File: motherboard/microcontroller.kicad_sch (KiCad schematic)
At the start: 5 parts, among them SW1 SW_Push, SW2 SW_Push, U3 ESP32-S3-WROOM-1

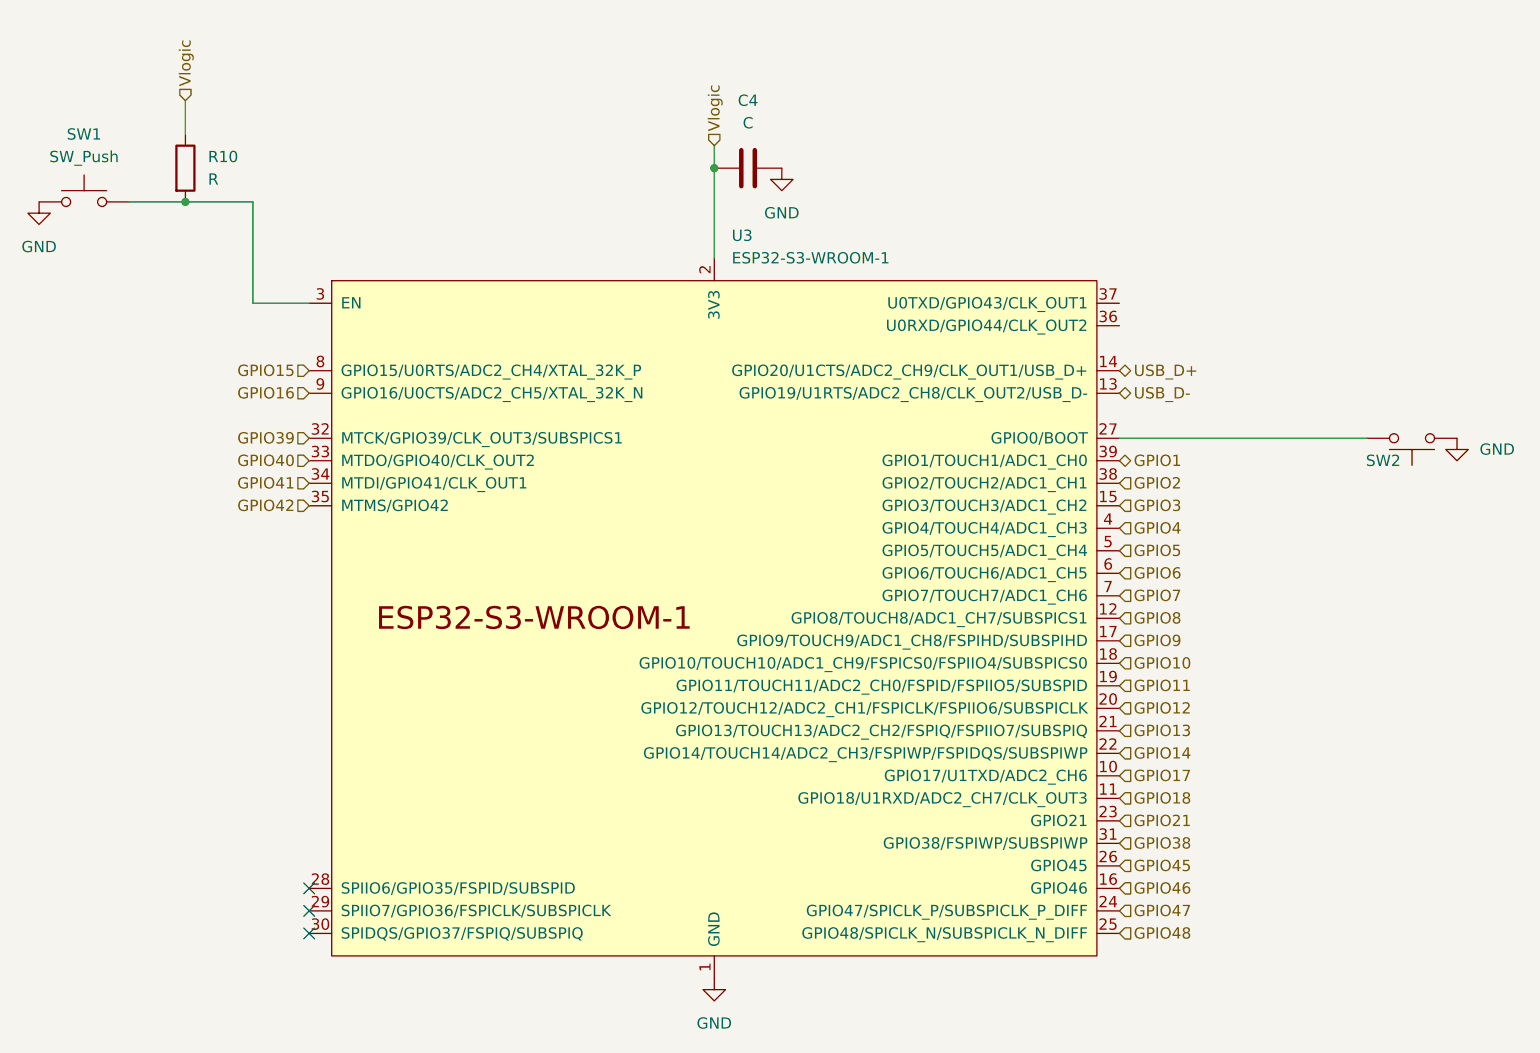
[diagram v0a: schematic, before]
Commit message: motherboard basics routed
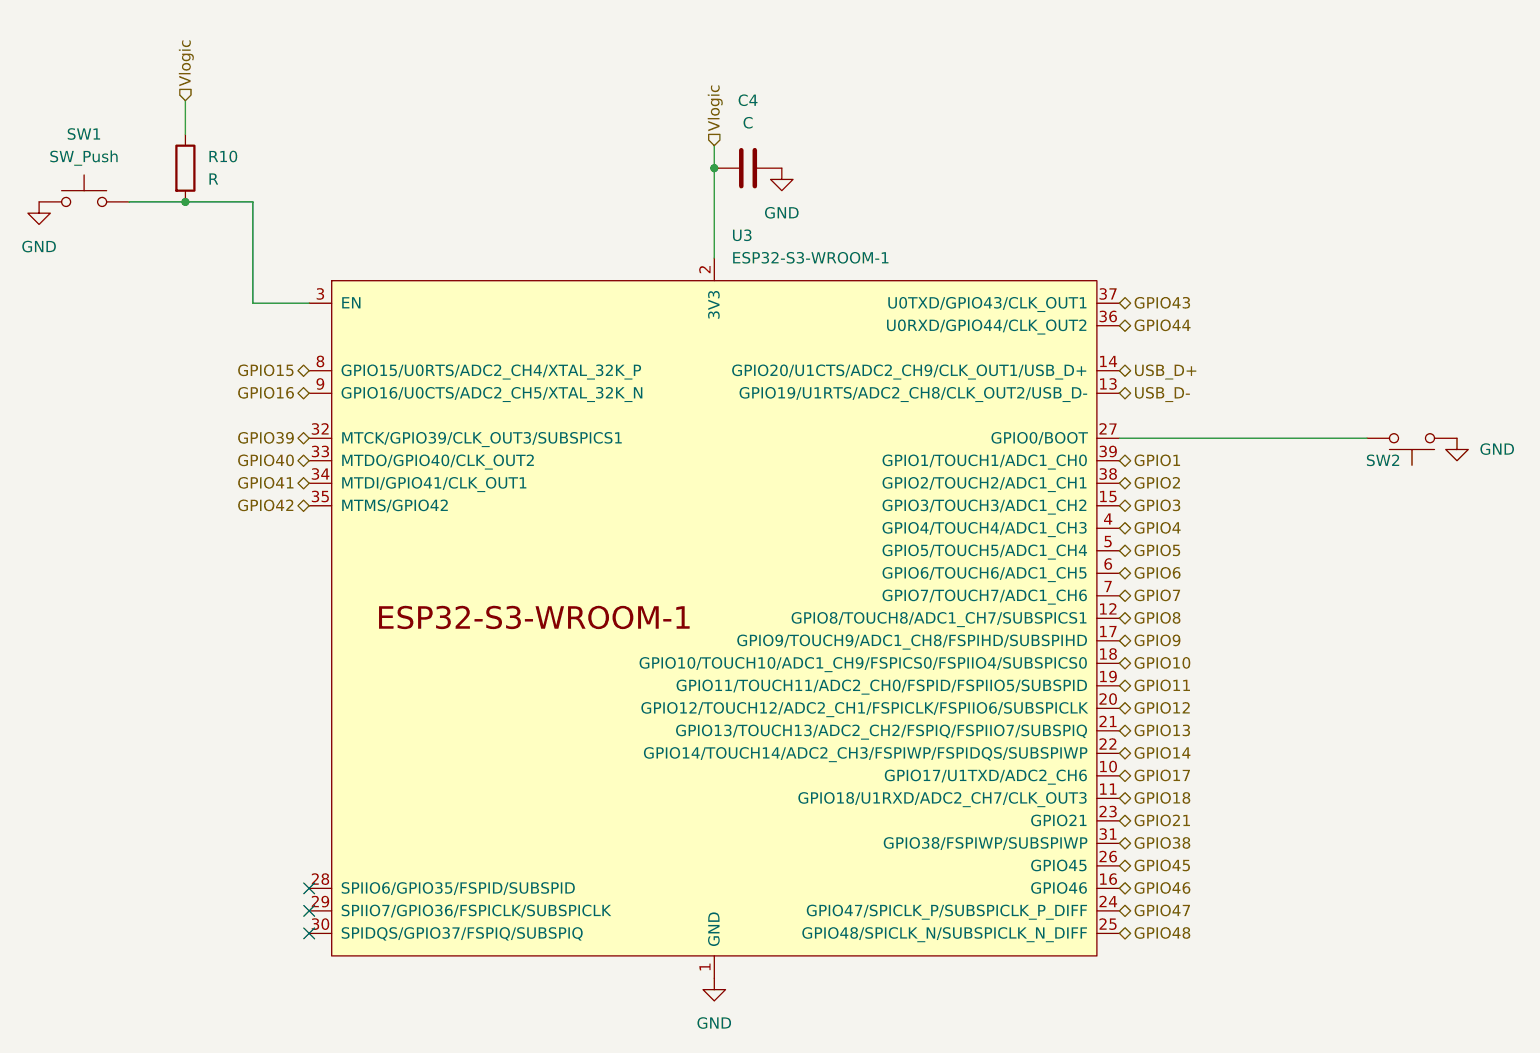
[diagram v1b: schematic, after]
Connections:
- net GPIO44: now reaches U3.36 (U0RXD/GPIO44/CLK_OUT2)
- net GPIO43: now reaches U3.37 (U0TXD/GPIO43/CLK_OUT1)
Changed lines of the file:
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@@
     (stroke (width 0) (type default))
   )
-  (hierarchical_label "GPIO47" (shape input) (at 162.56 148.59 0) (fields_autoplaced)
+  (hierarchical_label "GPIO47" (shape bidirectional) (at 162.56 148.59 0) (fields_autoplaced)
     (effects (font (size 1.27 1.27)) (justify left))
   )
@@
     (effects (font (size 1.27 1.27)) (justify left))
   )
-  (hierarchical_label "GPIO17" (shape input) (at 162.56 133.35 0) (fields_autoplaced)
+  (hierarchical_label "GPIO17" (shape bidirectional) (at 162.56 133.35 0) (fields_autoplaced)
     (effects (font (size 1.27 1.27)) (justify left))
   )
-  (hierarchical_label "GPIO11" (shape input) (at 162.56 123.19 0) (fields_autoplaced)
+  (hierarchical_label "GPIO11" (shape bidirectional) (at 162.56 123.19 0) (fields_autoplaced)
     (effects (font (size 1.27 1.27)) (justify left))
   )
-  (hierarchical_label "GPIO41" (shape input) (at 71.12 100.33 180) (fields_autoplaced)
+  (hierarchical_label "GPIO41" (shape bidirectional) (at 71.12 100.33 180) (fields_autoplaced)
     (effects (font (size 1.27 1.27)) (justify right))
   )
-  (hierarchical_label "GPIO18" (shape input) (at 162.56 135.89 0) (fields_autoplaced)
+  (hierarchical_label "GPIO18" (shape bidirectional) (at 162.56 135.89 0) (fields_autoplaced)
     (effects (font (size 1.27 1.27)) (justify left))
   )
-  (hierarchical_label "GPIO6" (shape input) (at 162.56 110.49 0) (fields_autoplaced)
+  (hierarchical_label "GPIO6" (shape bidirectional) (at 162.56 110.49 0) (fields_autoplaced)
     (effects (font (size 1.27 1.27)) (justify left))
   )
-  (hierarchical_label "GPIO48" (shape input) (at 162.56 151.13 0) (fields_autoplaced)
+  (hierarchical_label "GPIO43" (shape bidirectional) (at 162.56 80.01 0) (fields_autoplaced)
     (effects (font (size 1.27 1.27)) (justify left))
   )
-  (hierarchical_label "GPIO7" (shape input) (at 162.56 113.03 0) (fields_autoplaced)
+  (hierarchical_label "GPIO48" (shape bidirectional) (at 162.56 151.13 0) (fields_autoplaced)
     (effects (font (size 1.27 1.27)) (justify left))
   )
-  (hierarchical_label "GPIO45" (shape input) (at 162.56 143.51 0) (fields_autoplaced)
+  (hierarchical_label "GPIO7" (shape bidirectional) (at 162.56 113.03 0) (fields_autoplaced)
     (effects (font (size 1.27 1.27)) (justify left))
   )
-  (hierarchical_label "GPIO10" (shape input) (at 162.56 120.65 0) (fields_autoplaced)
+  (hierarchical_label "GPIO45" (shape bidirectional) (at 162.56 143.51 0) (fields_autoplaced)
     (effects (font (size 1.27 1.27)) (justify left))
   )
-  (hierarchical_label "GPIO4" (shape input) (at 162.56 105.41 0) (fields_autoplaced)
+  (hierarchical_label "GPIO10" (shape bidirectional) (at 162.56 120.65 0) (fields_autoplaced)
     (effects (font (size 1.27 1.27)) (justify left))
   )
-  (hierarchical_label "GPIO9" (shape input) (at 162.56 118.11 0) (fields_autoplaced)
+  (hierarchical_label "GPIO4" (shape bidirectional) (at 162.56 105.41 0) (fields_autoplaced)
     (effects (font (size 1.27 1.27)) (justify left))
   )
-  (hierarchical_label "GPIO13" (shape input) (at 162.56 128.27 0) (fields_autoplaced)
+  (hierarchical_label "GPIO9" (shape bidirectional) (at 162.56 118.11 0) (fields_autoplaced)
     (effects (font (size 1.27 1.27)) (justify left))
   )
-  (hierarchical_label "GPIO3" (shape input) (at 162.56 102.87 0) (fields_autoplaced)
+  (hierarchical_label "GPIO13" (shape bidirectional) (at 162.56 128.27 0) (fields_autoplaced)
     (effects (font (size 1.27 1.27)) (justify left))
   )
-  (hierarchical_label "GPIO38" (shape input) (at 162.56 140.97 0) (fields_autoplaced)
+  (hierarchical_label "GPIO3" (shape bidirectional) (at 162.56 102.87 0) (fields_autoplaced)
+    (effects (font (size 1.27 1.27)) (justify left))
+  )
+  (hierarchical_label "GPIO38" (shape bidirectional) (at 162.56 140.97 0) (fields_autoplaced)
     (effects (font (size 1.27 1.27)) (justify left))
   )
@@
     (effects (font (size 1.27 1.27)) (justify left))
   )
-  (hierarchical_label "GPIO5" (shape input) (at 162.56 107.95 0) (fields_autoplaced)
+  (hierarchical_label "GPIO5" (shape bidirectional) (at 162.56 107.95 0) (fields_autoplaced)
     (effects (font (size 1.27 1.27)) (justify left))
   )
-  (hierarchical_label "GPIO42" (shape input) (at 71.12 102.87 180) (fields_autoplaced)
+  (hierarchical_label "GPIO44" (shape bidirectional) (at 162.56 82.55 0) (fields_autoplaced)
+    (effects (font (size 1.27 1.27)) (justify left))
+  )
+  (hierarchical_label "GPIO42" (shape bidirectional) (at 71.12 102.87 180) (fields_autoplaced)
     (effects (font (size 1.27 1.27)) (justify right))
   )
-  (hierarchical_label "GPIO8" (shape input) (at 162.56 115.57 0) (fields_autoplaced)
+  (hierarchical_label "GPIO8" (shape bidirectional) (at 162.56 115.57 0) (fields_autoplaced)
     (effects (font (size 1.27 1.27)) (justify left))
   )
-  (hierarchical_label "GPIO21" (shape input) (at 162.56 138.43 0) (fields_autoplaced)
+  (hierarchical_label "GPIO21" (shape bidirectional) (at 162.56 138.43 0) (fields_autoplaced)
     (effects (font (size 1.27 1.27)) (justify left))
   )
-  (hierarchical_label "GPIO46" (shape input) (at 162.56 146.05 0) (fields_autoplaced)
+  (hierarchical_label "GPIO46" (shape bidirectional) (at 162.56 146.05 0) (fields_autoplaced)
     (effects (font (size 1.27 1.27)) (justify left))
   )
-  (hierarchical_label "GPIO14" (shape input) (at 162.56 130.81 0) (fields_autoplaced)
+  (hierarchical_label "GPIO14" (shape bidirectional) (at 162.56 130.81 0) (fields_autoplaced)
     (effects (font (size 1.27 1.27)) (justify left))
   )
-  (hierarchical_label "GPIO39" (shape input) (at 71.12 95.25 180) (fields_autoplaced)
+  (hierarchical_label "GPIO39" (shape bidirectional) (at 71.12 95.25 180) (fields_autoplaced)
     (effects (font (size 1.27 1.27)) (justify right))
   )
-  (hierarchical_label "GPIO15" (shape input) (at 71.12 87.63 180) (fields_autoplaced)
+  (hierarchical_label "GPIO15" (shape bidirectional) (at 71.12 87.63 180) (fields_autoplaced)
     (effects (font (size 1.27 1.27)) (justify right))
   )
-  (hierarchical_label "GPIO2" (shape input) (at 162.56 100.33 0) (fields_autoplaced)
+  (hierarchical_label "GPIO2" (shape bidirectional) (at 162.56 100.33 0) (fields_autoplaced)
     (effects (font (size 1.27 1.27)) (justify left))
   )
-  (hierarchical_label "GPIO12" (shape input) (at 162.56 125.73 0) (fields_autoplaced)
+  (hierarchical_label "GPIO12" (shape bidirectional) (at 162.56 125.73 0) (fields_autoplaced)
     (effects (font (size 1.27 1.27)) (justify left))
   )
-  (hierarchical_label "GPIO16" (shape input) (at 71.12 90.17 180) (fields_autoplaced)
+  (hierarchical_label "GPIO16" (shape bidirectional) (at 71.12 90.17 180) (fields_autoplaced)
     (effects (font (size 1.27 1.27)) (justify right))
   )
-  (hierarchical_label "GPIO40" (shape input) (at 71.12 97.79 180) (fields_autoplaced)
+  (hierarchical_label "GPIO40" (shape bidirectional) (at 71.12 97.79 180) (fields_autoplaced)
     (effects (font (size 1.27 1.27)) (justify right))
   )

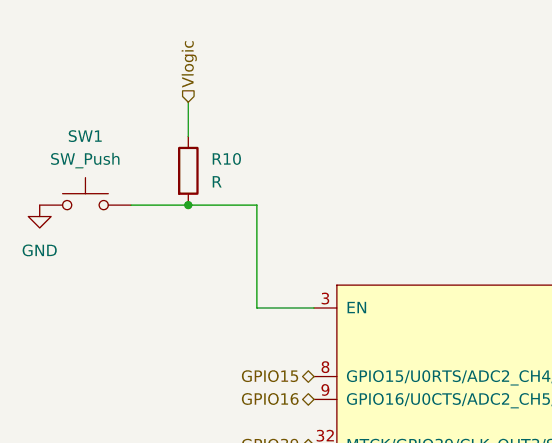
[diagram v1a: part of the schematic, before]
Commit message: reroute motherboard: no traces under antenna
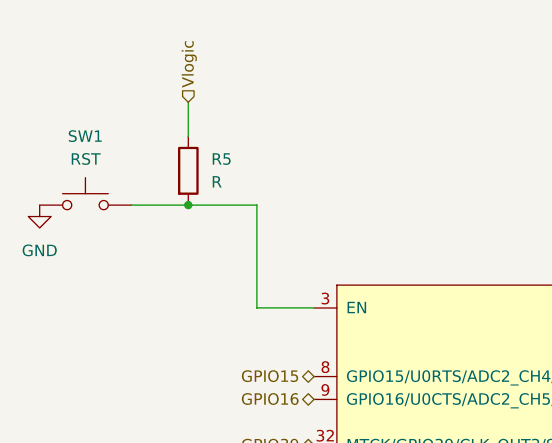
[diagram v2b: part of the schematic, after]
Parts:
- SW1: value SW_Push -> RST
- SW2: value SW_Push -> BOOT
- renumbered R10 to R5
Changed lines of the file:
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@@
       (effects (font (size 1.27 1.27)))
     )
-    (property "Value" "SW_Push" (at 45.72 63.5 0)
+    (property "Value" "RST" (at 45.72 63.5 0)
       (effects (font (size 1.27 1.27)))
     )
@@
   (symbol (lib_id "Device:R") (at 57.15 64.77 0) (unit 1)
     (in_bom yes) (on_board yes) (dnp no) (fields_autoplaced)
-    (property "Reference" "R10" (at 59.69 63.5 0)
+    (property "Reference" "R5" (at 59.69 63.5 0)
       (effects (font (size 1.27 1.27)) (justify left))
     )
@@
       (project "motherboard"
         (path "/e63e39d7-6ac0-4ffd-8aa3-1841a4541b55/631e97d5-0781-48b4-a71b-4d5a2ac6a098"
-          (reference "R10") (unit 1)
+          (reference "R5") (unit 1)
         )
       )
@@
       (effects (font (size 1.27 1.27)) (justify left))
     )
-    (property "Value" "SW_Push" (at 193.04 103.886 0)
+    (property "Value" "BOOT" (at 193.04 103.886 0)
       (effects (font (size 1.27 1.27)) hide)
     )
